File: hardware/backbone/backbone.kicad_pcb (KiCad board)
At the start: 4 copper layers, 31.3 x 68.9 mm, 72 parts, among them J1 M20-7810645R, J140 M20-7810645R, J2 FROM_PREVIOUS, J3 M20-7810645R, J4 SM04B-SRSS-TB(LF)(SN), J5 FH12-24S-0.5SH(55), J9 TO NEXT, Q2 AO3401A, U1 ESP32-S3-WROOM-1_1U_FlexyPin_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, U2 SN65HVD230DR, U3 HC-TYPE-C-16P-01A, U4 AP2112K-3.3TRG1, U5 AP2112K-3.3TRG1, U8 G3VM-61VY3

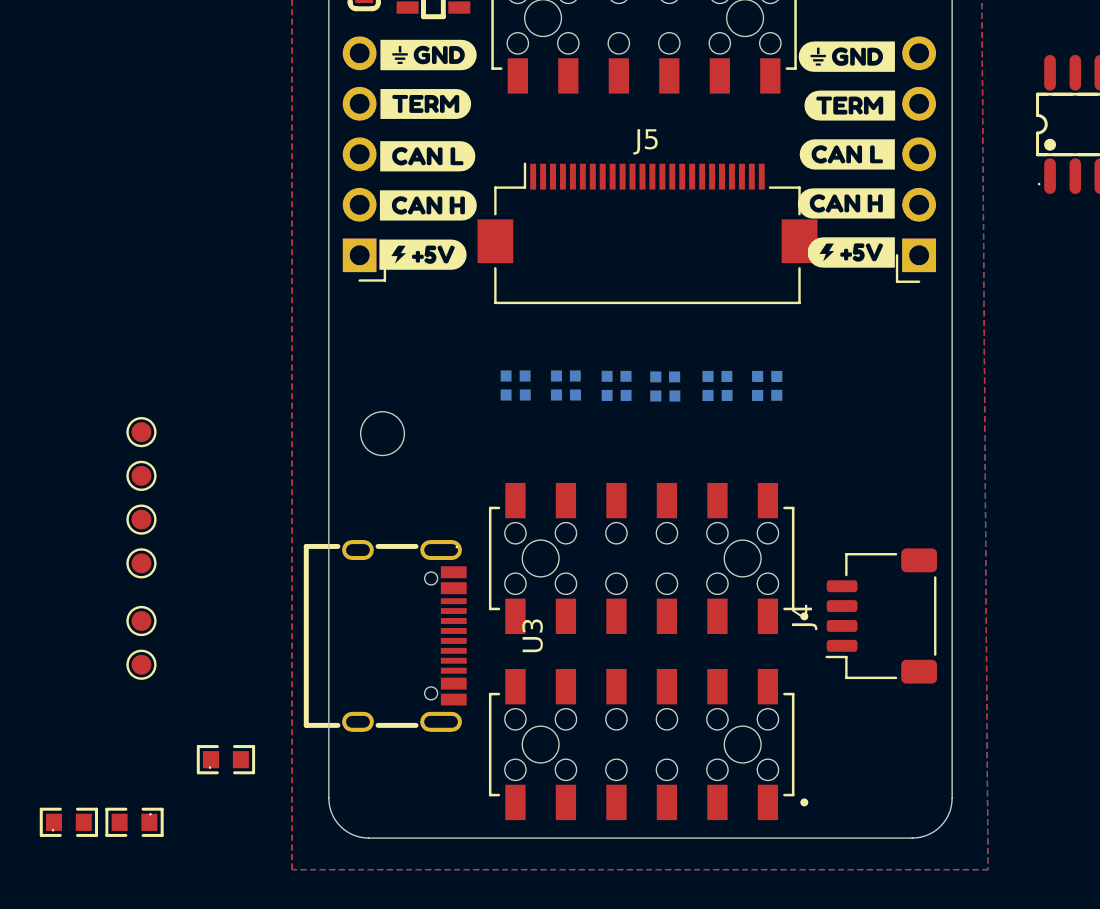
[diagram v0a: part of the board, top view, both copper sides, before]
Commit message: Update V3 LED layout for hand-formed MINI-E and solid FR4 windows
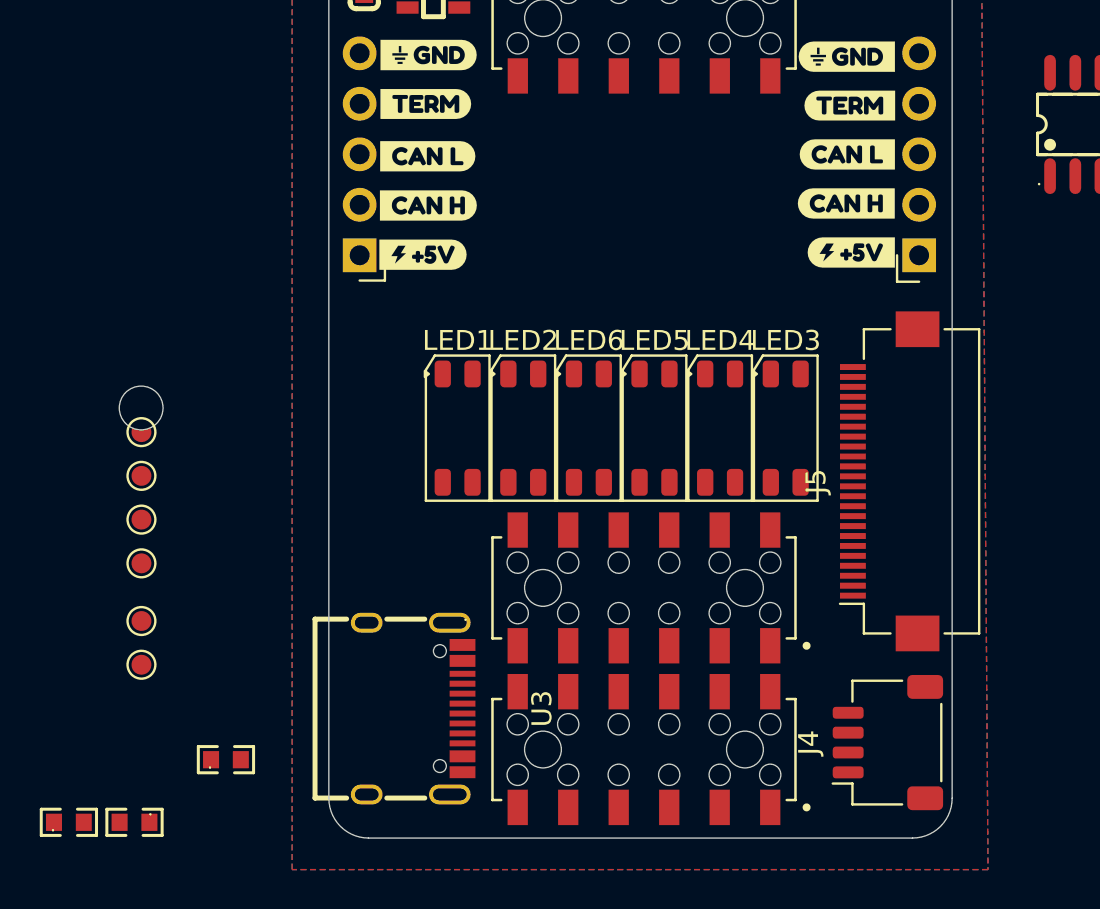
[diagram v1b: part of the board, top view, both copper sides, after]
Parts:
- LED1, LED2, LED3, LED4, LED5, LED6: value SK6805-EC15 -> SK6812MINI-E; footprint SpaghettiLABold:LED-SMD_4P-L1.5-W1.5-BL -> SpaghettiLAB:LED_SK6812MINI-E_FR4_Window_HandFormed; moved to F.Cu
- moved J5 18.2 mm to (180.1, 113.5), turned to 90 degrees
- moved LED1 15.7 mm to (158.4, 110.8)
- moved LED3 13.7 mm to (174.9, 110.8), turned to 180 degrees
- moved H4 12.2 mm to (142.5, 109.8)
- moved LED2 10.00 mm to (161.7, 110.8), turned to 180 degrees
- moved LED4 8.05 mm to (171.6, 110.8), turned to 180 degrees
- moved J4 6.37 mm to (180.0, 126.6)
- moved LED6 4.38 mm to (165.0, 110.8), turned to 180 degrees
- moved U3 3.68 mm to (156.2, 124.9)
- moved LED5 2.86 mm to (168.3, 110.8), turned to 180 degrees
- moved J1 1.48 mm to (167.8, 118.9)
- moved J140 0.28 mm to (167.8, 127.0)
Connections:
- LED1 pad 1: ALED -> GND
- LED1 pad 2: VAUX -> ALED
- LED1 pad 3: Net-(LED1-DOUT) -> VAUX
- LED1 pad 4: GND -> Net-(LED1-DOUT)
- LED2 pad 1: Net-(LED1-DOUT) -> GND
- LED2 pad 2: VAUX -> Net-(LED1-DOUT)
- LED2 pad 3: Net-(LED2-DOUT) -> VAUX
- LED2 pad 4: GND -> Net-(LED2-DOUT)
- LED3 pad 1: Net-(LED2-DOUT) -> GND
- LED3 pad 2: VAUX -> Net-(LED2-DOUT)
- LED3 pad 3: Net-(LED3-DOUT) -> VAUX
- LED3 pad 4: GND -> Net-(LED3-DOUT)
- LED4 pad 1: Net-(LED3-DOUT) -> GND
- LED4 pad 2: VAUX -> Net-(LED3-DOUT)
- LED4 pad 3: Net-(LED4-DOUT) -> VAUX
- LED4 pad 4: GND -> Net-(LED4-DOUT)
- LED5 pad 1: Net-(LED4-DOUT) -> GND
- LED5 pad 2: VAUX -> Net-(LED4-DOUT)
- LED5 pad 3: Net-(LED5-DOUT) -> VAUX
- LED5 pad 4: GND -> Net-(LED5-DOUT)
- LED6 pad 1: Net-(LED5-DOUT) -> GND
- LED6 pad 2: VAUX -> Net-(LED5-DOUT)
- LED6 pad 3: unconnected-(LED6-DOUT-Pad3) -> VAUX
- LED6 pad 4: GND -> unconnected-(LED6-DOUT-Pad3)

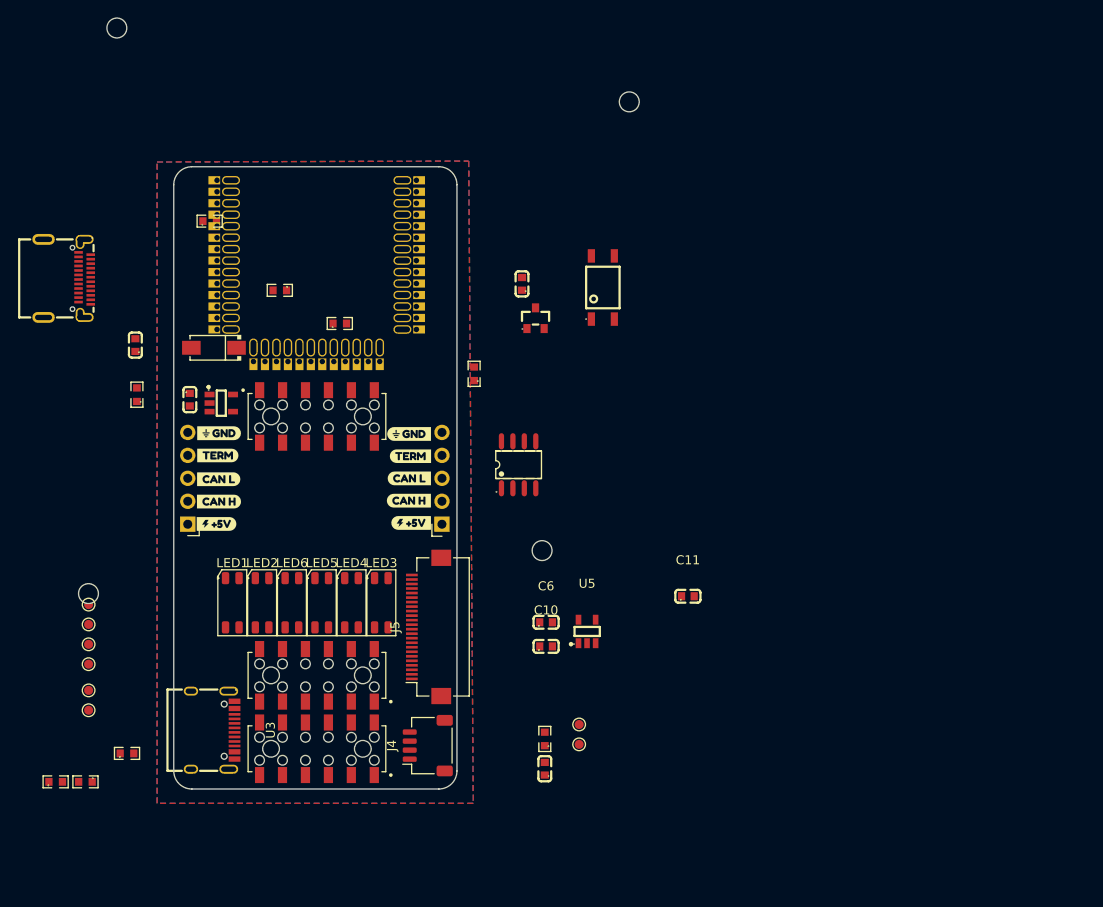
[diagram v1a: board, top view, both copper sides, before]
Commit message: Update V3 power supply and dual-face magnetic edge contacts
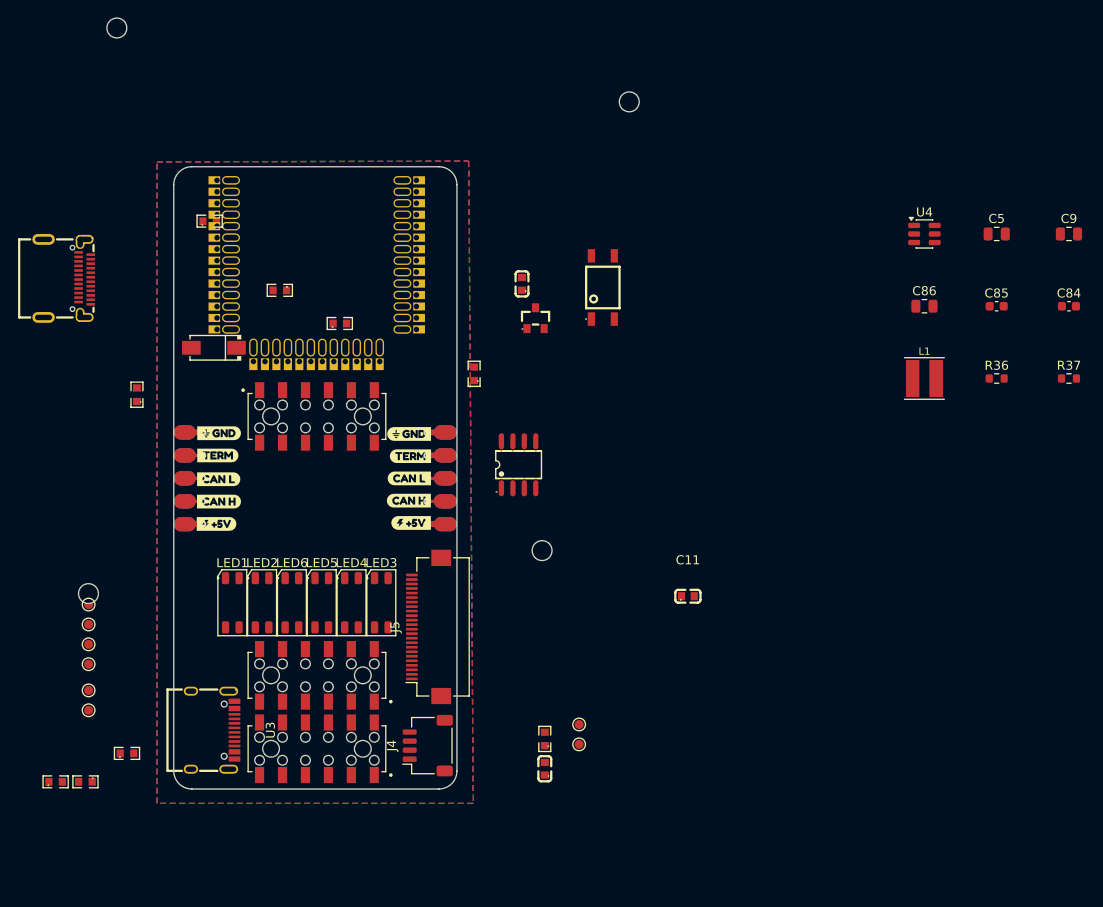
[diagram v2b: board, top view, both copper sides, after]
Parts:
- removed C10, C6: 1uF, SpaghettiLAB:C0603
- removed U5: AP2112K-3.3TRG1, SpaghettiLAB:SOT-25-5_L2.9-W1.6-P0.95-LS2.8-BL
- added C84: 100nF/50V, Capacitor_SMD:C_0603_1608Metric, F.Cu at (251.0, 78.0)
- added C85: 100nF/50V, Capacitor_SMD:C_0603_1608Metric, F.Cu at (243.0, 78.0)
- added C86: 22uF, Capacitor_SMD:C_0805_2012Metric, F.Cu at (235.0, 78.0)
- added L1: 3.3uH, SpaghettiLAB:L_XRTC404012S, F.Cu at (235.0, 86.0)
- added R36: 33k 1%, Resistor_SMD:R_0603_1608Metric, F.Cu at (243.0, 86.0)
- added R37: 10k 1%, Resistor_SMD:R_0603_1608Metric, F.Cu at (251.0, 86.0)
- C5, C9: value 1uF -> 22uF; footprint SpaghettiLAB:C0603 -> Capacitor_SMD:C_0805_2012Metric
- J2: footprint Connector_PinSocket_2.54mm:PinSocket_1x05_P2.54mm_Horizontal -> SpaghettiLAB:Magnetic_J2_Edge_DualFace
- J9: footprint Connector_PinHeader_2.54mm:PinHeader_1x05_P2.54mm_Horizontal -> SpaghettiLAB:Magnetic_J9_Edge_DualFace
- U4: value AP2112K-3.3TRG1 -> TPS562201DDCR; footprint SpaghettiLAB:SOT-25-5_L2.9-W1.6-P0.95-LS2.8-BL -> SpaghettiLAB:TSOT-23-6_Power
- moved C9 104.1 mm to (251.0, 70.0), turned to 0 degrees
- moved C5 91.2 mm to (243.0, 70.0), turned to 0 degrees
- moved U4 80.1 mm to (235.0, 70.0), turned to 0 degrees
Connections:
- C5 pad 1: GND -> 5V
- C5 pad 2: 5V -> GND
- C9 pad 1: GND -> VCORE
- C9 pad 2: VCORE -> GND
- LED1 pad 3: VAUX -> VCORE
- LED2 pad 3: VAUX -> VCORE
- LED3 pad 3: VAUX -> VCORE
- LED4 pad 3: VAUX -> VCORE
- LED5 pad 3: VAUX -> VCORE
- LED6 pad 3: VAUX -> VCORE
- U4 pad 1: 5V -> GND
- U4 pad 2: GND -> Net-(U4-SW)
- U4 pad 4: unconnected-(U4-NC-Pad4) -> Net-(U4-VFB)
- U4 pad 5: VCORE -> 5V
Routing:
- net 5V: track 0.00 -> 9.90 mm, vias 0 -> 3
- net GND: track 0.00 -> 6.60 mm, vias 0 -> 2
- net CAN_L: track 0.00 -> 6.60 mm, vias 0 -> 2
- net CAN_H: track 0.00 -> 6.60 mm, vias 0 -> 2
- net TERM_CTRL_OUT: track 0.00 -> 3.30 mm, vias 0 -> 1
